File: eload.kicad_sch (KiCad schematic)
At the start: 62 parts, among them J1 Device Power, J2 Input, J3 JST Header, J4 SWD Header, J6 JST Header, J7 Conn_02x06_Odd_Even, K1 G5Q-1, Q1 TIP122, Q2 NMOS, Q3 DTC043Z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

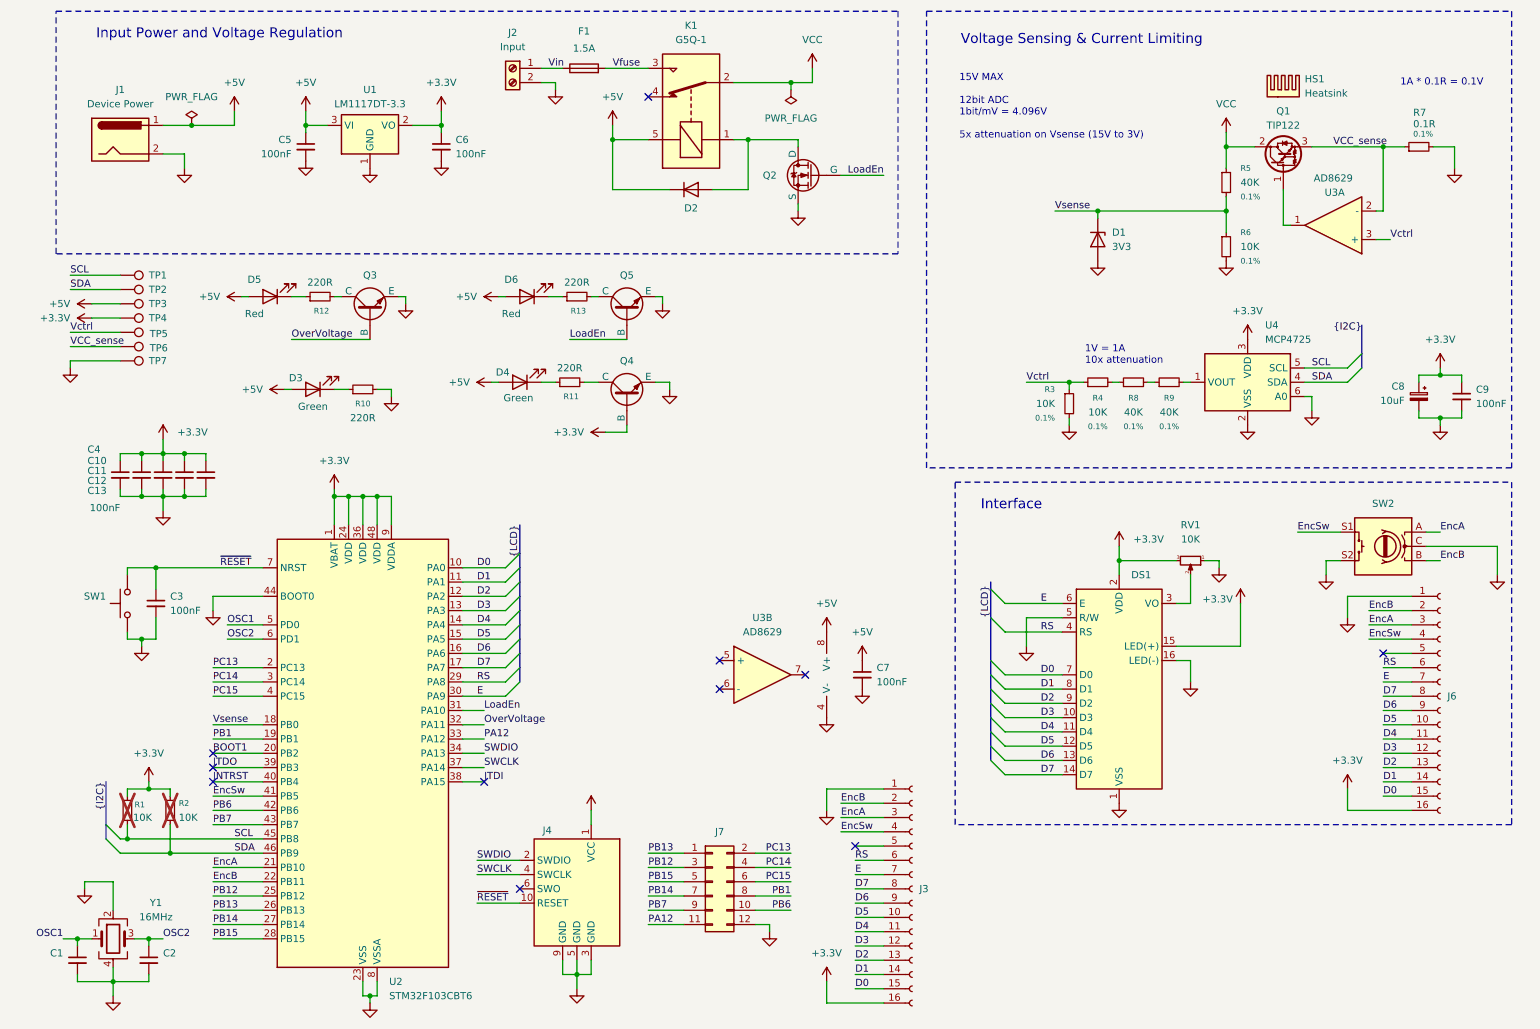
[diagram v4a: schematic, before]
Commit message: Split schematics into 2 pages
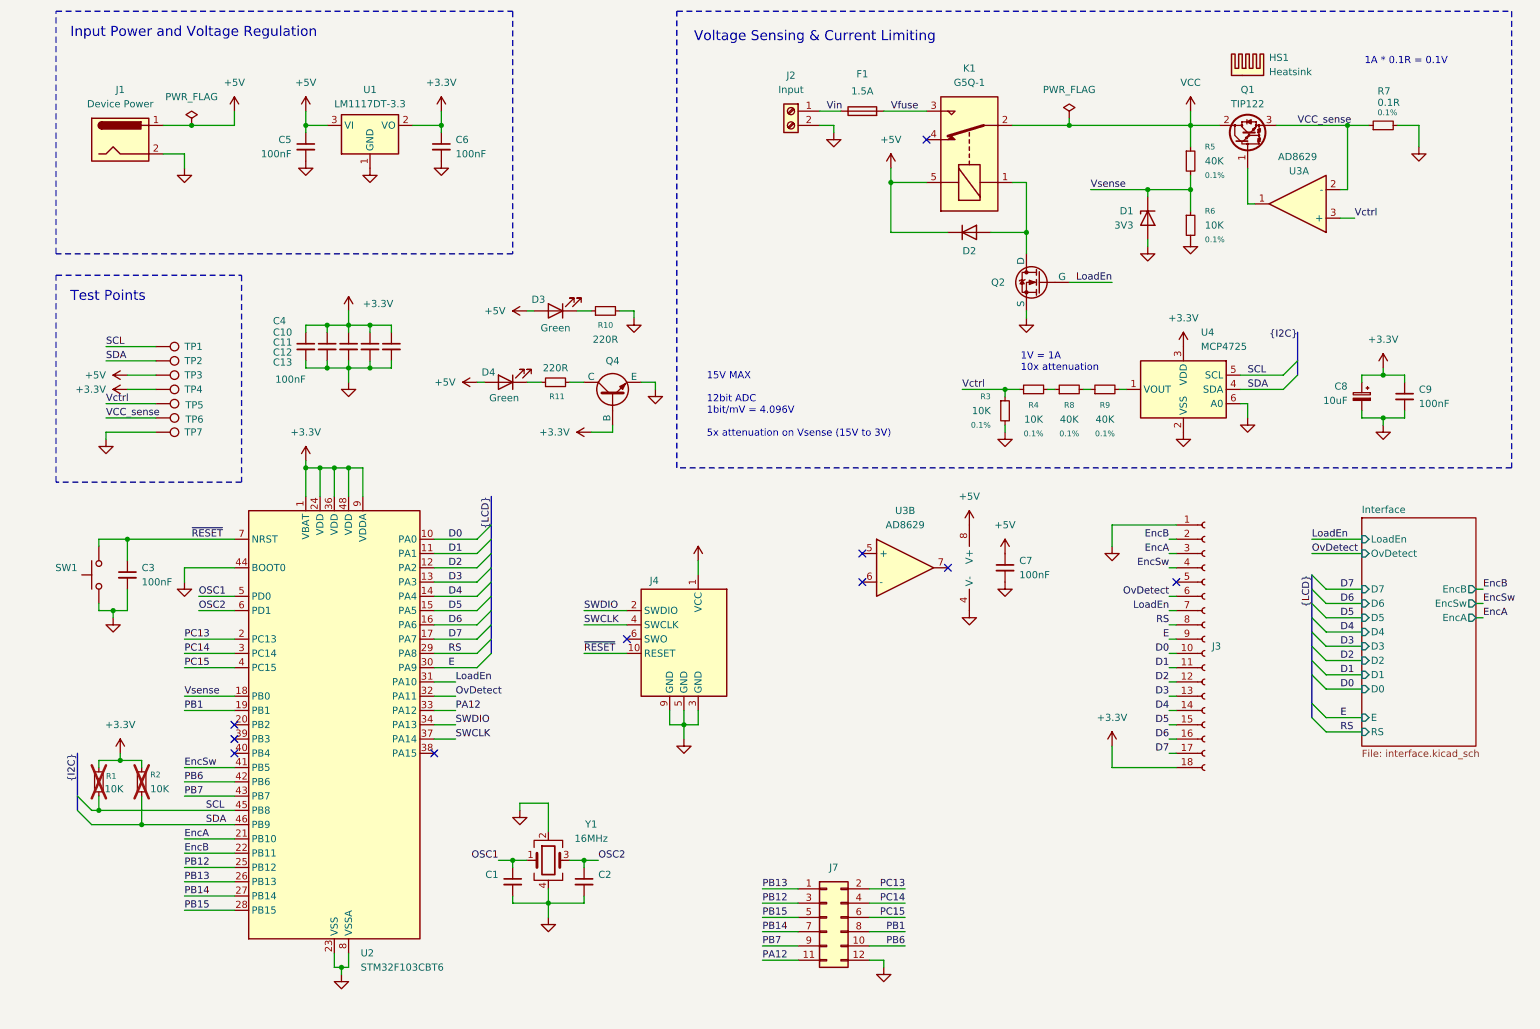
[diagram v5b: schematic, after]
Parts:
- removed D5, D6: 17-215/GHC-YR1S2/4T, LED_SMD:LED_0805_2012Metric_Pad1.15x1.40mm_HandSolder, symbol Device:LED
- removed DS1: WC1602A, Display:WC1602A, symbol Display_Character:WC1602A
- removed J3, J6: JST Header, Connector_JST:JST_XH_B16B-XH-A_1x16_P2.50mm_Vertical, symbol Connector:Conn_01x16_Socket
- removed Q3, Q5: DTC043Z, symbol Simulation_SPICE:NPN
- removed R12, R13: 220R, symbol Device:R_Small
- removed RV1: 10K, Potentiometer_THT:Potentiometer_Bourns_3266W_Vertical, symbol Device:R_Potentiometer_Small
- removed SW2: RotaryEncoder_Switch, Rotary_Encoder:RotaryEncoder_Bourns_Vertical_PEC12R-3x17F-Sxxxx, symbol Device:RotaryEncoder_Switch
- added J3: JST Header, Connector_JST:JST_XH_B16B-XH-A_1x16_P2.50mm_Vertical, symbol Connector:Conn_01x18_Socket
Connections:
- net +3.3V: now also J3.18 (Pin_18)
- net D0: now also J3.10 (Pin_10)
- net D1: now also J3.11 (Pin_11)
- net D2: now also J3.12 (Pin_12)
- net D3: now also J3.13 (Pin_13)
- net D4: now also J3.14 (Pin_14)
- net D5: now also J3.15 (Pin_15)
- net D6: now also J3.16 (Pin_16)
- net D7: now also J3.17 (Pin_17)
- net E: now also J3.9 (Pin_9)
- net EncA: now also J3.3 (Pin_3)
- net EncB: now also J3.2 (Pin_2)
- net EncSw: now also J3.4 (Pin_4)
- net GND: now also J3.1 (Pin_1)
- net LoadEn: now also J3.7 (Pin_7)
- net RS: now also J3.8 (Pin_8)
- net BOOT1: no longer names the net of U2.20 (PB2)
- net JNTRST: no longer names the net of U2.40 (PB4)
- net JTDI: no longer names the net of U2.38 (PA15)
- net JTDO: no longer names the net of U2.39 (PB3)
- net OverVoltage renamed OvDetect
- net OvDetect: now also J3.6 (Pin_6)
- no-connect marks 11 -> 10
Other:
- added sheet Interface (interface.kicad_sch)
- note added: "Test Points"
- note removed: "Interface"
- moved on the sheet: C1, C10, C11, C12, C13, C2, C3, C4, C7, C8, C9, D1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

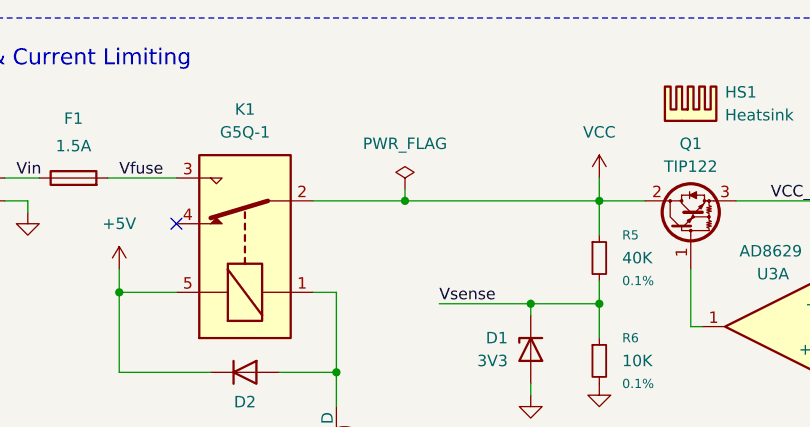
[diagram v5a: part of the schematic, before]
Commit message: EMF supressing diode and relay MOSFET has been choosed
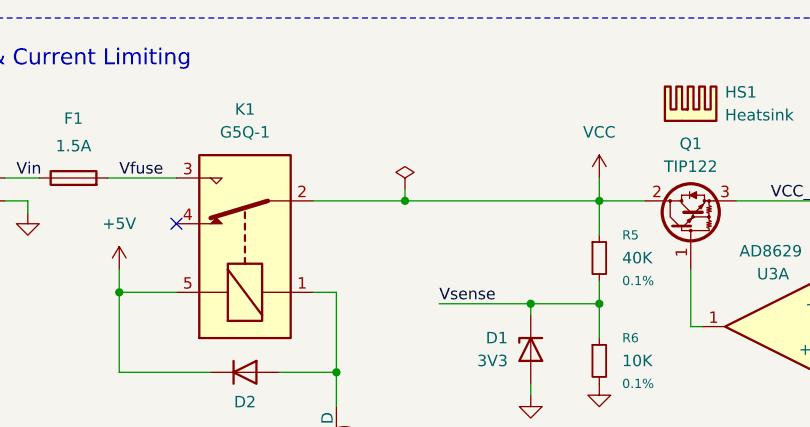
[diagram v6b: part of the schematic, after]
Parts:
- D1: LCSC Part # C19077437 -> C507913
- D2: value D -> MBR120VLSFT1G; LCSC Part # (none) -> C223608
- Q2: value NMOS -> HL 40N05; footprint (none) -> Package_TO_SOT_SMD:SOT-23-3; LCSC Part # (none) -> C7543825
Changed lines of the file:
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@@
 		(on_board yes)
 		(dnp no)
-		(fields_autoplaced yes)
 		(property "Reference" "K1"
 			(at 180.34 27.94 90)
@@
 			)
 		)
-		(property "Datasheet" "https://www.lcsc.com/datasheet/C19077437.pdf"
+		(property "Datasheet" "https://www.lcsc.com/datasheet/C507913.pdf"
 			(at 212.09 54.61 0)
 			(effects
@@
 			)
 		)
-		(property "LCSC Part #" "C19077437"
+		(property "LCSC Part #" "C507913"
 			(at 212.09 54.61 90)
 			(effects
@@
 					(size 1.27 1.27)
 				)
+				(hide yes)
 			)
 		)
@@
 			)
 		)
-		(property "Value" "NMOS"
+		(property "Value" "HL 40N05"
 			(at 186.69 67.3099 0)
 			(effects
@@
 			)
 		)
-		(property "Footprint" ""
+		(property "Footprint" "Package_TO_SOT_SMD:SOT-23-3"
 			(at 187.96 63.5 0)
 			(effects
@@
 			)
 		)
-		(property "Datasheet" "https://ngspice.sourceforge.io/docs/ngspice-html-manual/manual.xhtml#cha_MOSFETs"
+		(property "Datasheet" "https://www.lcsc.com/datasheet/C7543825.pdf"
 			(at 193.04 78.74 0)
 			(effects
@@
 			)
 		)
-		(property "Description" "N-MOSFET transistor, drain/source/gate"
+		(property "Description" ""
 			(at 193.04 66.04 0)
 			(effects
@@
 			)
 		)
+		(property "LCSC Part #" "C7543825"
+			(at 193.04 66.04 0)
+			(effects
+				(font
+					(size 1.27 1.27)
+				)
+				(hide yes)
+			)
+		)
 		(pin "3"
 		)
@@
 			)
 		)
-		(property "Value" "D"
+		(property "Value" "MBR120VLSFT1G"
 			(at 180.34 60.96 0)
 			(effects
@@
 			)
 		)
-		(property "Datasheet" "~"
+		(property "Datasheet" "https://www.lcsc.com/datasheet/C223608.pdf"
 			(at 180.34 57.15 0)
 			(effects
@@
 			)
 		)
-		(property "Description" "Diode"
+		(property "Description" "20V 1A Vf=0.3V"
 			(at 180.34 57.15 0)
 			(effects
@@
 			(at 180.34 57.15 0)
 			(effects
+				(font
+					(size 1.27 1.27)
+				)
+				(hide yes)
+			)
+		)
+		(property "LCSC Part #" "C223608"
+			(at 180.34 57.15 0)
+			(effects

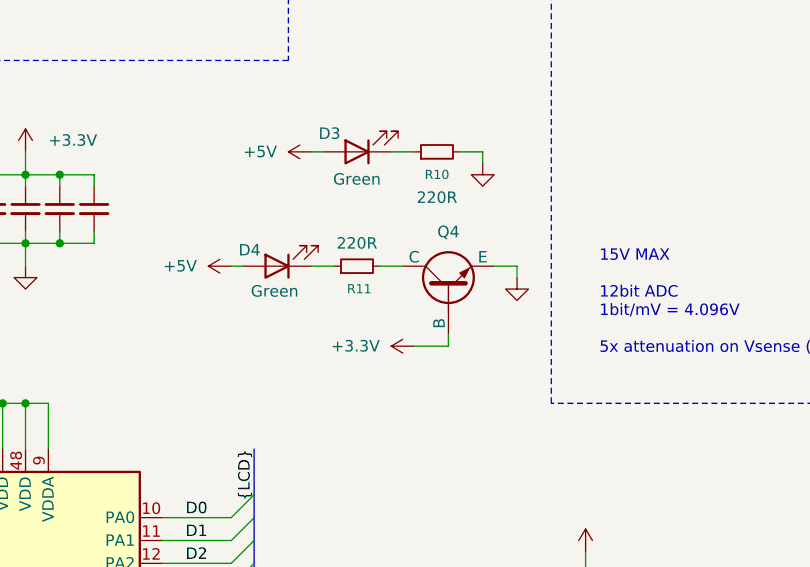
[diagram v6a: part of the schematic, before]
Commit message: Biased NPN transistor correct schematic symbol, Resistor values
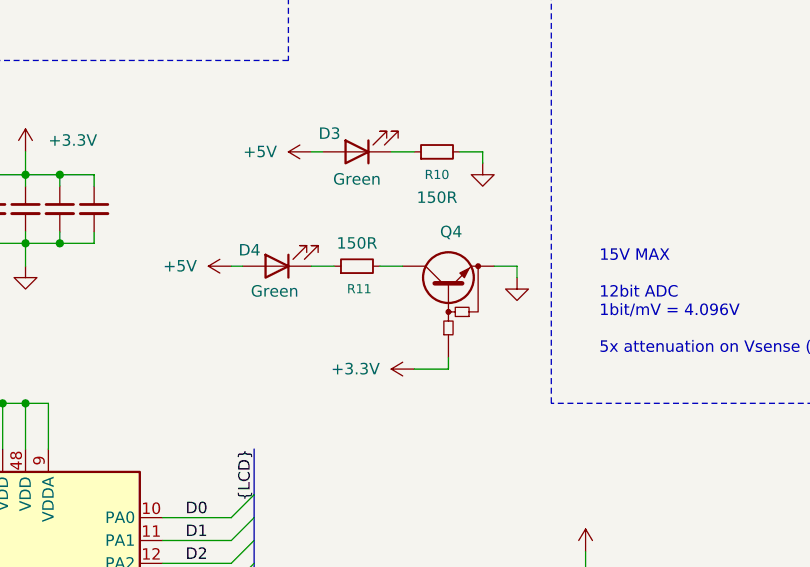
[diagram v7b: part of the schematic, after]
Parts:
- Q4: symbol Simulation_SPICE:NPN -> Device:Q_NPN_BRT
- R10, R11: value 220R -> 150R; footprint (none) -> Resistor_SMD:R_0805_2012Metric_Pad1.20x1.40mm_HandSolder; LCSC Part # (none) -> C844818
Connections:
- net +3.3V: now also Q4.B; no longer Q4.2 (B)
- net GND: now also Q4.E; no longer Q4.3 (E)
- net at R11.2: now also Q4.C; no longer Q4.1 (C)
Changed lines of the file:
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@@
 	(wire
 		(pts
-			(xy 116.84 92.71) (xy 113.03 92.71)
+			(xy 116.84 95.25) (xy 113.03 95.25)
 		)
 		(stroke
@@
 	(wire
 		(pts
-			(xy 116.84 91.44) (xy 116.84 92.71)
+			(xy 116.84 93.98) (xy 116.84 95.25)
 		)
 		(stroke
@@
 	(symbol
 		(lib_id "power:+3.3V")
-		(at 113.03 92.71 90)
+		(at 113.03 95.25 90)
 		(unit 1)
 		(exclude_from_sim no)
@@
 		(fields_autoplaced yes)
 		(property "Reference" "#PWR059"
-			(at 116.84 92.71 0)
+			(at 116.84 95.25 0)
 			(effects
 				(font
@@
 		)
 		(property "Value" "+3.3V"
-			(at 109.22 92.7099 90)
+			(at 109.22 95.2499 90)
 			(effects
 				(font
@@
 		)
 		(property "Footprint" ""
-			(at 113.03 92.71 0)
+			(at 113.03 95.25 0)
 			(effects
 				(font
@@
 		)
 		(property "Datasheet" ""
-			(at 113.03 92.71 0)
+			(at 113.03 95.25 0)
 			(effects
 				(font
@@
 		)
 		(property "Description" "Power symbol creates a global label with name \"+3.3V\""
-			(at 113.03 92.71 0)
+			(at 113.03 95.25 0)
 			(effects
 				(font
@@
 	)
 	(symbol
-		(lib_id "Simulation_SPICE:NPN")
-		(at 116.84 86.36 90)
+		(lib_id "Device:Q_NPN_BRT")
+		(at 116.84 85.09 90)
 		(unit 1)
 		(exclude_from_sim no)
@@
 		(fields_autoplaced yes)
 		(property "Reference" "Q4"
-			(at 116.84 80.01 90)
+			(at 117.1448 80.01 90)
 			(effects
 				(font
@@
 		)
 		(property "Value" "DTC043Z"
-			(at 116.84 80.01 90)
+			(at 116.84 78.74 90)
 			(effects
 				(font
@@
 		)
 		(property "Footprint" ""
-			(at 116.84 22.86 0)
+			(at 116.84 21.59 0)
 			(effects
 				(font
@@
 		)
 		(property "Datasheet" "https://www.lcsc.com/datasheet/C96459.pdf"
-			(at 116.84 22.86 0)
+			(at 116.84 21.59 0)
 			(effects
 				(font
@@
 		)
 		(property "Description" ""
-			(at 116.84 86.36 0)
-			(effects
-				(font
-					(size 1.27 1.27)
-				)
-				(hide yes)
-			)
-		)
-		(property "Sim.Device" "NPN"
-			(at 116.84 86.36 0)
-			(effects
-				(font
-					(size 1.27 1.27)
-				)
-				(hide yes)
-			)
-		)
-		(property "Sim.Type" "GUMMELPOON"
-			(at 116.84 86.36 0)
-			(effects
-				(font
-					(size 1.27 1.27)
-				)
-				(hide yes)
-			)
-		)
-		(property "Sim.Pins" "1=C 2=B 3=E"
-			(at 116.84 86.36 0)
+			(at 116.84 85.09 0)
 			(effects
 				(font
@@
 		)
 		(property "LCSC Part #" "C96459"
-			(at 116.84 86.36 90)
+			(at 116.84 85.09 90)
 			(effects
 				(font
@@
 			)
 		)
-		(pin "2"
+		(pin "B"
 		)
-		(pin "3"
+		(pin "C"
 		)
-		(pin "1"
+		(pin "E"
 		)
 		(instances
@@
 			)
 		)
-		(property "Datasheet" "~"
+		(property "Datasheet" "https://www.lcsc.com/datasheet/C110775.pdf"
 			(at 33.02 154.94 0)
 			(effects
@@
 			)
 		)
-		(property "Datasheet" "~"
+		(property "Datasheet" "https://www.lcsc.com/datasheet/C110775.pdf"
 			(at 25.4 154.94 0)
 			(effects
@@
 			)
 		)
-		(property "Value" "220R"
+		(property "Value" "150R"
 			(at 106.68 81.28 90)
 			(effects
@@
 			)
 		)
-		(property "Footprint" ""
+		(property "Footprint" "Resistor_SMD:R_0805_2012Metric_Pad1.20x1.40mm_HandSolder"
 			(at 106.68 83.82 0)
 			(effects
@@
 			)
 		)
-		(property "Datasheet" "~"
+		(property "Datasheet" "https://www.lcsc.com/datasheet/C844818.pdf"
 			(at 106.68 83.82 0)
 			(effects
@@
 			)
 		)
-		(property "Description" "Resistor, small symbol"
+		(property "Description" "VISHAY CRCW0805150RFKEA"
 			(at 106.68 83.82 0)
 			(effects
@@
 			)
 		)
+		(property "LCSC Part #" "C844818"
+			(at 106.68 83.82 90)
+			(effects
+				(font
+					(size 1.27 1.27)
+				)
+				(hide yes)
+			)
+		)
 		(pin "1"
 		)
@@
 			)
 		)
-		(property "Value" "220R"
+		(property "Value" "150R"
 			(at 115.57 76.2 90)
 			(effects
@@
 			)
 		)
-		(property "Footprint" ""
+		(property "Footprint" "Resistor_SMD:R_0805_2012Metric_Pad1.20x1.40mm_HandSolder"
 			(at 115.57 71.12 0)
 			(effects
@@
 			)
 		)
-		(property "Datasheet" "~"
+		(property "Datasheet" "https://www.lcsc.com/datasheet/C844818.pdf"
 			(at 115.57 71.12 0)
 			(effects
@@
 			)
 		)
-		(property "Description" "Resistor, small symbol"
+		(property "Description" "VISHAY CRCW0805150RFKEA"
 			(at 115.57 71.12 0)
 			(effects
 				(font
+					(size 1.27 1.27)
+				)
+				(hide yes)
+			)
+		)
+		(property "LCSC Part #" "C844818"
+			(at 115.57 71.12 90)
+			(effects
+				(font
